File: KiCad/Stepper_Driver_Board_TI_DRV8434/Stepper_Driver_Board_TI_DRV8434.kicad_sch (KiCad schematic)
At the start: 25 parts, among them J1 Motor Connect, J2 PWR & DATA Connect, J3 Battery Connect, SW1 SW_SPDT_MSM, SW2 SW_SPDT_MSM, U1 DRV8434PWPR, U2 PC817, U4 6N137, U6 PC817

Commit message: worked on layout
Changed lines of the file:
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@@
 (kicad_sch
-	(version 20231120)
+	(version 20250114)
 	(generator "eeschema")
-	(generator_version "8.0")
+	(generator_version "9.0")
 	(paper "A4")
 	(junction
@@
 	(label "ENA_ESP"
 		(at 260.35 48.26 0)
-		(fields_autoplaced yes)
 		(effects
 			(font
@@
 	(label "AOUT1"
 		(at 85.09 76.2 0)
-		(fields_autoplaced yes)
 		(effects
 			(font
@@
 	(label "CPL"
 		(at 161.29 68.58 0)
-		(fields_autoplaced yes)
 		(effects
 			(font
@@
 	(label "CPH"
 		(at 161.29 66.04 0)
-		(fields_autoplaced yes)
 		(effects
 			(font
@@
 	(label "M1"
 		(at 172.72 81.28 0)
-		(fields_autoplaced yes)
 		(effects
 			(font
@@
 	(label "ENA"
 		(at 161.29 73.66 0)
-		(fields_autoplaced yes)
 		(effects
 			(font
@@
 	(label "PUL"
 		(at 161.29 78.74 0)
-		(fields_autoplaced yes)
 		(effects
 			(font
@@
 	(label "AOUT2"
 		(at 85.09 78.74 0)
-		(fields_autoplaced yes)
 		(effects
 			(font
@@
 	(label "BOUT2"
 		(at 85.09 81.28 0)
-		(fields_autoplaced yes)
 		(effects
 			(font
@@
 	(label "DIR_ESP"
 		(at 260.35 50.8 0)
-		(fields_autoplaced yes)
-		(effects
-			(font
-				(size 1.27 1.27)
-			)
-			(justify left bottom)
-		)
-	)
-	(label "PAD"
-		(at 158.75 63.5 0)
-		(fields_autoplaced yes)
 		(effects
 			(font
@@
 	(label "DIR"
 		(at 161.29 76.2 0)
-		(fields_autoplaced yes)
 		(effects
 			(font
@@
 	(label "M0"
 		(at 172.72 91.44 0)
-		(fields_autoplaced yes)
 		(effects
 			(font
@@
 	(label "DECAY0"
 		(at 158.75 83.82 0)
-		(fields_autoplaced yes)
 		(effects
 			(font
@@
 	(label "DECAY1"
 		(at 160.02 88.9 0)
-		(fields_autoplaced yes)
 		(effects
 			(font
@@
 	(label "BOUT1"
 		(at 85.09 83.82 0)
-		(fields_autoplaced yes)
 		(effects
 			(font
@@
 	(label "VREF"
 		(at 172.72 93.98 0)
-		(fields_autoplaced yes)
 		(effects
 			(font
@@
 	(label "FAULT"
 		(at 160.02 96.52 0)
-		(fields_autoplaced yes)
 		(effects
 			(font
@@
 	(label "PUL_ESP"
 		(at 260.35 53.34 0)
-		(fields_autoplaced yes)
 		(effects
 			(font
@@
 	(label "VCP"
 		(at 106.68 58.42 0)
-		(fields_autoplaced yes)
 		(effects
 			(font
@@
 		(length 2.54)
 		(shape round)
-		(at 110.49 102.87 90)
+		(at 251.46 106.68 0)
 		(fields_autoplaced yes)
 		(effects
@@
 			(justify left bottom)
 		)
+		(property "Netclass" "+BATT"
+			(at 252.1585 104.14 0)
+			(effects
+				(font
+					(size 1.27 1.27)
+					(italic yes)
+				)
+				(justify left)
+			)
+		)
+	)
+	(netclass_flag ""
+		(length 2.54)
+		(shape round)
+		(at 251.46 109.22 180)
+		(fields_autoplaced yes)
+		(effects
+			(font
+				(size 1.27 1.27)
+			)
+			(justify right bottom)
+		)
 		(property "Netclass" "GND"
-			(at 107.95 102.1715 90)
+			(at 252.1585 111.76 0)
 			(effects
 				(font
@@
 	)
 	(symbol
-		(lib_id "DRV8434:DRV8434PWPR")
-		(at 113.03 63.5 0)
-		(unit 1)
-		(exclude_from_sim no)
-		(in_bom yes)
-		(on_board yes)
-		(dnp no)
-		(fields_autoplaced yes)
-		(property "Reference" "U1"
-			(at 135.89 53.34 0)
-			(effects
-				(font
-					(size 1.524 1.524)
-				)
-			)
-		)
-		(property "Value" "DRV8434PWPR"
-			(at 135.89 55.88 0)
-			(effects
-				(font
-					(size 1.524 1.524)
-				)
-			)
-		)
-		(property "Footprint" "TSSOP_34PWPR_TEX"
-			(at 133.35 47.498 0)
-			(effects
-				(font
-					(size 1.27 1.27)
-					(italic yes)
-				)
-				(hide yes)
-			)
-		)
-		(property "Datasheet" "https://www.ti.com/lit/gpn/drv8434"
-			(at 130.81 49.784 0)
-			(effects
-				(font
-					(size 1.27 1.27)
-					(italic yes)
-				)
-				(hide yes)
-			)
-		)
-		(property "Description" ""
-			(at 113.03 63.5 0)
-			(effects
-				(font
-					(size 1.27 1.27)
-				)
-				(hide yes)
-			)
-		)
-		(pin "22"
-		)
-		(pin "24"
-		)
-		(pin "23"
-		)
-		(pin "20"
-		)
-		(pin "EPAD"
-		)
-		(pin "4"
-		)
-		(pin "6"
-		)
-		(pin "1"
-		)
-		(pin "21"
-		)
-		(pin "7"
-		)
-		(pin "2"
-		)
-		(pin "28"
-		)
-		(pin "27"
-		)
-		(pin "3"
-		)
-		(pin "17"
-		)
-		(pin "19"
-		)
-		(pin "11"
-		)
-		(pin "12"
-		)
-		(pin "10"
-		)
-		(pin "18"
-		)
-		(pin "25"
-		)
-		(pin "9"
-		)
-		(pin "8"
-		)
-		(pin "5"
-		)
-		(pin "16"
-		)
-		(pin "14"
-		)
-		(pin "15"
-		)
-		(pin "13"
-		)
-		(pin "26"
-		)
-		(instances
-			(project ""
-				(path "/04678f1c-4410-4048-912a-66017db83283"
-					(reference "U1")
-					(unit 1)
-				)
-			)
-		)
-	)
-	(symbol
 		(lib_id "Device:R")
 		(at 240.03 31.75 270)
@@
 	)
 	(symbol
+		(lib_id "DRV8434:DRV8434PWPR")
+		(at 113.03 63.5 0)
+		(unit 1)
+		(exclude_from_sim no)
+		(in_bom yes)
+		(on_board yes)
+		(dnp no)
+		(fields_autoplaced yes)
+		(property "Reference" "U1"
+			(at 135.89 53.34 0)
+			(effects
+				(font
+					(size 1.524 1.524)
+				)
+			)
+		)
+		(property "Value" "DRV8434PWPR"
+			(at 135.89 55.88 0)
+			(effects
+				(font
+					(size 1.524 1.524)
+				)
+			)
+		)
+		(property "Footprint" "TSSOP_34PWPR_TEX"
+			(at 113.03 63.5 0)
+			(effects
+				(font
+					(size 1.27 1.27)
+					(italic yes)
+				)
+				(hide yes)
+			)
+		)
+		(property "Datasheet" "https://www.ti.com/lit/gpn/drv8434"
+			(at 113.03 63.5 0)
+			(effects
+				(font
+					(size 1.27 1.27)
+					(italic yes)
+				)
+				(hide yes)
+			)
+		)
+		(property "Description" ""
+			(at 113.03 63.5 0)
+			(effects
+				(font
+					(size 1.27 1.27)
+				)
+				(hide yes)
+			)
+		)
+		(pin "19"
+		)
+		(pin "1"
+		)
+		(pin "15"
+		)
+		(pin "20"
+		)
+		(pin "21"
+		)
+		(pin "2"
+		)
+		(pin "12"
+		)
+		(pin "13"
+		)
+		(pin "11"
+		)
+		(pin "3"
+		)
+		(pin "27"
+		)
+		(pin "25"
+		)
+		(pin "28"
+		)
+		(pin "24"
+		)
+		(pin "16"
+		)
+		(pin "26"
+		)
+		(pin "17"
+		)
+		(pin "7"
+		)
+		(pin "6"
+		)
+		(pin "18"
+		)
+		(pin "4"
+		)
+		(pin "5"
+		)
+		(pin "8"
+		)
+		(pin "10"
+		)
+		(pin "9"
+		)
+		(pin "14"
+		)
+		(pin "EPAD"
+		)
+		(pin "22"
+		)
+		(pin "23"
+		)
+		(instances
+			(project ""
+				(path "/04678f1c-4410-4048-912a-66017db83283"
+					(reference "U1")
+					(unit 1)
+				)
+			)
+		)
+	)
+	(symbol
 		(lib_id "power:GND")
 		(at 160.02 106.68 0)
@@
 		)
 	)
+	(embedded_fonts no)
 )

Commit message: Finished Rough Layout!
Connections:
- net ENA_ESP: now also J2.5 (Pin_5); no longer J2.3 (Pin_3)
- net PUL_ESP: now also J2.3 (Pin_3); no longer J2.5 (Pin_5)
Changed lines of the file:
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@@
 	(wire
 		(pts
-			(xy 256.54 80.01) (xy 248.92 80.01)
+			(xy 254 80.01) (xy 248.92 80.01)
 		)
 		(stroke
@@
 	(wire
 		(pts
-			(xy 256.54 48.26) (xy 256.54 26.67)
-		)
-		(stroke
-			(width 0)
-			(type default)
-		)
-	)
-	(wire
-		(pts
 			(xy 189.23 109.22) (xy 189.23 110.49)
 		)
@@
 	(wire
 		(pts
-			(xy 256.54 53.34) (xy 256.54 80.01)
+			(xy 254 48.26) (xy 254 80.01)
 		)
 		(stroke
@@
 	(wire
 		(pts
-			(xy 256.54 53.34) (xy 275.59 53.34)
-		)
-		(stroke
-			(width 0)
-			(type default)
-		)
-	)
-	(wire
-		(pts
 			(xy 246.38 106.68) (xy 254 106.68)
 		)
@@
 	(wire
 		(pts
+			(xy 259.08 53.34) (xy 275.59 53.34)
+		)
+		(stroke
+			(width 0)
+			(type default)
+		)
+	)
+	(wire
+		(pts
 			(xy 212.09 55.88) (xy 212.09 57.15)
 		)
@@
 	(wire
 		(pts
-			(xy 256.54 48.26) (xy 275.59 48.26)
-		)
-		(stroke
-			(width 0)
-			(type default)
-		)
-	)
-	(wire
-		(pts
 			(xy 166.37 55.88) (xy 166.37 66.04)
 		)
@@
 	(wire
 		(pts
-			(xy 256.54 26.67) (xy 233.68 26.67)
+			(xy 259.08 26.67) (xy 233.68 26.67)
 		)
 		(stroke
@@
 	(wire
 		(pts
+			(xy 259.08 26.67) (xy 259.08 53.34)
+		)
+		(stroke
+			(width 0)
+			(type default)
+		)
+	)
+	(wire
+		(pts
+			(xy 254 48.26) (xy 275.59 48.26)
+		)
+		(stroke
+			(width 0)
+			(type default)
+		)
+	)
+	(wire
+		(pts
 			(xy 214.63 49.53) (xy 214.63 50.8)
 		)
@@
 	)
 	(label "ENA_ESP"
-		(at 260.35 48.26 0)
+		(at 260.35 53.34 0)
 		(effects
 			(font
@@
 		)
 	)
+	(label "PUL_ESP"
+		(at 260.35 48.26 0)
+		(effects
+			(font
+				(size 1.27 1.27)
+			)
+			(justify left bottom)
+		)
+	)
 	(label "DIR"
 		(at 161.29 76.2 0)
@@
 		(effects
 			(font
-				(size 1.27 1.27)
-			)
-			(justify left bottom)
-		)
-	)
-	(label "PUL_ESP"
-		(at 260.35 53.34 0)
-		(effects
-			(font

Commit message: driver board updating
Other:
- moved on the sheet: C1, C2, C3, C4, C5, C6, C7, J1, J2, J3, R1, R2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

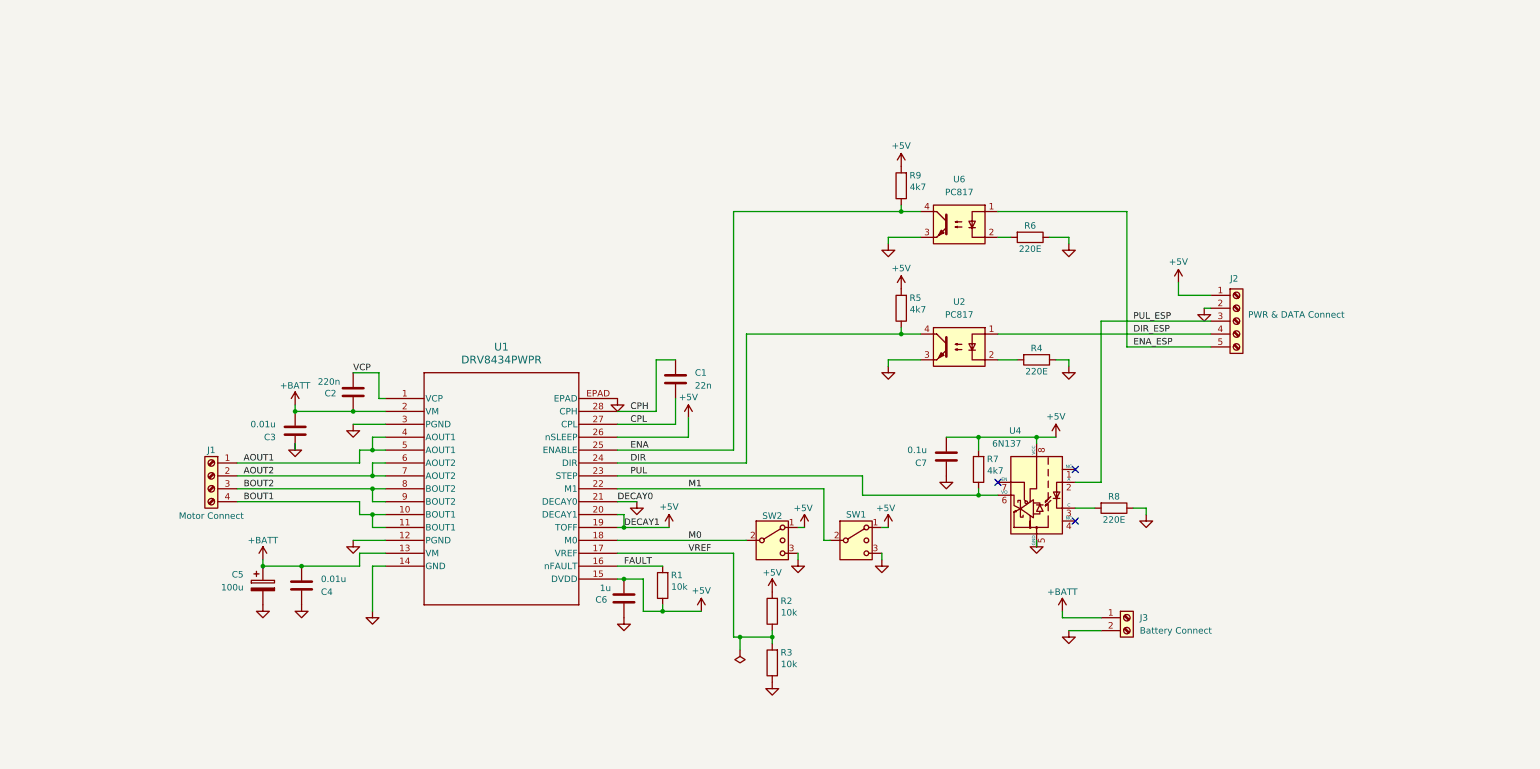
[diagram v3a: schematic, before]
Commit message: Added Ground Plane and stiching vias
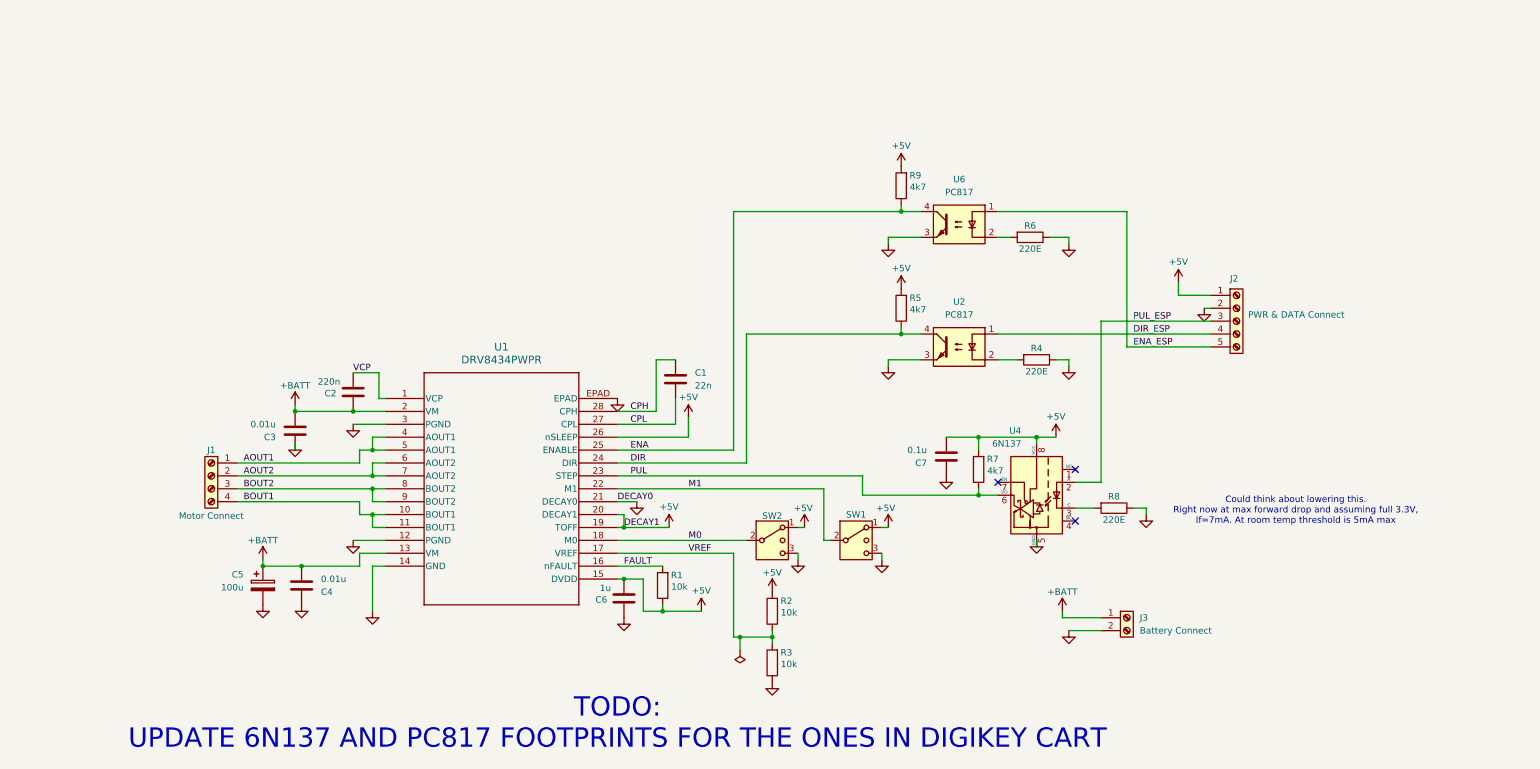
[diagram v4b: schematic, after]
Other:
- note added: "Could think about lowering this. Right now at max forward drop and assuming full 3.3V, If=7mA. At room temp threshold is 5mA max"
- note added: "TODO: UPDATE 6N137 AND PC817 FOOTPRINTS FOR THE ONES IN DIGIKEY CART"
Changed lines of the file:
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@@
 	(generator_version "9.0")
 	(paper "A4")
+	(text "Could think about lowering this. \nRight now at max forward drop and assuming full 3.3V, \nIf=7mA. At room temp threshold is 5mA max\n"
+		(exclude_from_sim no)
+		(at 260.604 110.998 0)
+		(effects
+			(font
+				(size 1.27 1.27)
+			)
+		)
+	)
+	(text "TODO:\nUPDATE 6N137 AND PC817 FOOTPRINTS FOR THE ONES IN DIGIKEY CART"
+		(exclude_from_sim no)
+		(at 127 152.908 0)
+		(effects
+			(font
+				(size 3.81 3.81)
+			)
+		)
+	)
 	(junction
 		(at 128.27 124.46)

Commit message: Needs some more work on 2esp
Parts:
- U1: footprint TSSOP_34PWPR_TEX -> DRV8434PWPR:TSSOP_34PWPR_TEX
- U4: footprint Package_DIP:DIP-8_W7.62mm -> 6n137:DIP762W60P254L968H450Q8N
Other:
- note removed: "TODO: UPDATE 6N137 AND PC817 FOOTPRINTS FOR THE ONES IN DIGIKEY CART"
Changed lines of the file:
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@@
 		)
 	)
-	(text "TODO:\nUPDATE 6N137 AND PC817 FOOTPRINTS FOR THE ONES IN DIGIKEY CART"
-		(exclude_from_sim no)
-		(at 127 152.908 0)
-		(effects
-			(font
-				(size 3.81 3.81)
-			)
-		)
-	)
 	(junction
 		(at 128.27 124.46)
@@
 			)
 		)
-		(property "Footprint" "Package_DIP:DIP-8_W7.62mm"
+		(property "Footprint" "6n137:DIP762W60P254L968H450Q8N"
 			(at 209.55 120.65 0)
 			(effects
@@
 			)
 		)
-		(property "Footprint" "TSSOP_34PWPR_TEX"
+		(property "Footprint" "DRV8434PWPR:TSSOP_34PWPR_TEX"
 			(at 81.28 88.9 0)
 			(effects
